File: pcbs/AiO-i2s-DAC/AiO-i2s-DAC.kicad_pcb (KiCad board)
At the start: 2 copper layers, 58.8 x 55.7 mm, 102 parts, among them J1 UART1, J2 SJ-3524-SMT-TR, J3 Audio Out, J4 UART0, J5 USB4105-GF-A, J6 USB4105-GF-A, J7 Conn_01x02, Q3 BC818, Q4 MBT3904DW1, Q6 MBT3904DW1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

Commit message: S3 insertion start
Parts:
- removed C10, C13, C15: 10uF 10V, Capacitor_SMD:C_0603_1608Metric
- removed C11, C14: 0.1uF 50V, Capacitor_SMD:C_0603_1608Metric
- removed D1, D11, D2, D9: 2.1V G 10mA, LED_SMD:LED_0603_1608Metric
- removed D14: 1N5819HW-7-F, DIY:SOD3716X145N
- removed D8: SP0503BAHTG, Package_TO_SOT_SMD:SOT-143
- removed DCD1, GND1: TestPoint_Small, TestPoint:TestPoint_Pad_D1.0mm
- removed J3: Audio Out, Connector_PinHeader_2.54mm:PinHeader_1x03_P2.54mm_Vertical
- removed J6: USB4105-GF-A, DIY:GCT_USB4105-GF-A
- removed JP1: ActDCD, Jumper:SolderJumper-3_P1.3mm_Bridged12_RoundedPad1.0x1.5mm
- removed R1, R2, R34, R35: 1K 1%, Resistor_SMD:R_0603_1608Metric
- removed R15, R23: 22.1K 1%, Resistor_SMD:R_0603_1608Metric
- removed R16, R24: 47.5K 1%, Resistor_SMD:R_0603_1608Metric
- removed R17, R25: 2K 1%, Resistor_SMD:R_0603_1608Metric
- removed R18, R19, R26, R27, R29: 0R, Resistor_SMD:R_0603_1608Metric
- removed R28, R30: 5.1K 1%, Resistor_SMD:R_0603_1608Metric
- removed U3, U4: CP2102-GM, Package_DFN_QFN:QFN-28-1EP_5x5mm_P0.5mm_EP3.35x3.35mm
- added D12: 2.1V G 10mA, LED_SMD:LED_0603_1608Metric, F.Cu at (213.5, 70.5)
- added D13: 2.1V G 10mA, LED_SMD:LED_0603_1608Metric, F.Cu at (213.5, 73.1)
- added D3: 2.1V G 10mA, LED_SMD:LED_0603_1608Metric, F.Cu at (213.5, 65.3)
- added D4: 2.1V G 10mA, LED_SMD:LED_0603_1608Metric, F.Cu at (213.5, 67.9)
- added DTR0: TestPoint_Small, TestPoint:TestPoint_Pad_D2.0mm, F.Cu at (209.4, 66.0)
- added HPD1: TestPoint_Small, TestPoint:TestPoint_Pad_D2.0mm, F.Cu at (209.4, 70.1)
- added JP4: HPD bypass, Jumper:SolderJumper-2_P1.3mm_Open_RoundedPad1.0x1.5mm, F.Cu at (217.6, 65.8)
- added R10: 1K 1%, Resistor_SMD:R_0603_1608Metric, F.Cu at (205.4, 70.3)
- added R11: 1K 1%, Resistor_SMD:R_0603_1608Metric, F.Cu at (205.4, 72.8)
- added R42: 10K 1%, Resistor_SMD:R_0603_1608Metric, F.Cu at (205.4, 75.3)
- added R43: 10K 1%, Resistor_SMD:R_0603_1608Metric, F.Cu at (205.4, 77.8)
- added R8: 1K 1%, Resistor_SMD:R_0603_1608Metric, F.Cu at (205.4, 65.3)
- added R9: 1K 1%, Resistor_SMD:R_0603_1608Metric, F.Cu at (205.4, 67.8)
- added RTS0: TestPoint_Small, TestPoint:TestPoint_Pad_D2.0mm, F.Cu at (209.4, 74.1)
- added U6: ESP32-S3, Package_DFN_QFN:QFN-56-1EP_7x7mm_P0.4mm_EP5.6x5.6mm, F.Cu at (216.1, 79.0)
- moved J4 39.1 mm to (213.0, 87.2)
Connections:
- net /CP2102_0/D+ renamed /usb_dp
- net /CP2102_0/D- renamed /usb_dn
- net Net-(C9-Pad2) renamed BOOT
- J1 pad 2: DCD -> AGND
- J2 pad TN: unconnected-(J2-PadTN) -> Net-(JP4-A)
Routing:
- net RXD1: track 67.9 -> 0.00 mm, vias 4 -> 0
- net +3.3V: track 183.6 -> 119.9 mm, vias 9 -> 2
- net TXD1: track 60.8 -> 3.66 mm, vias 6 -> 1
- net RXD0: track 42.9 -> 0.00 mm, vias 2 -> 0
- net DCD: track 42.7 -> 0.00 mm, vias 2 -> 0
- net TXD0: track 39.7 -> 0.00 mm, vias 2 -> 0
- net VBUS: track 55.4 -> 19.7 mm, vias 4 -> 2
- net DTR0: track 55.9 -> 22.2 mm, vias 3 -> 2
- net RTS0: track 47.8 -> 17.1 mm, vias 4 -> 3
- net Net-(J6-SHELL_GND): track 19.8 -> 0.00 mm
- net /CP2102-GM/D+: track 16.1 -> 0.00 mm, vias 3 -> 0
- net /CP2102-GM/D-: track 14.9 -> 0.00 mm, vias 2 -> 0
- net ROUT: track 18.9 -> 7.19 mm
- net LOUT: track 19.5 -> 13.9 mm
- net +5V: track 78.4 -> 73.2 mm, vias 3 -> 2
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
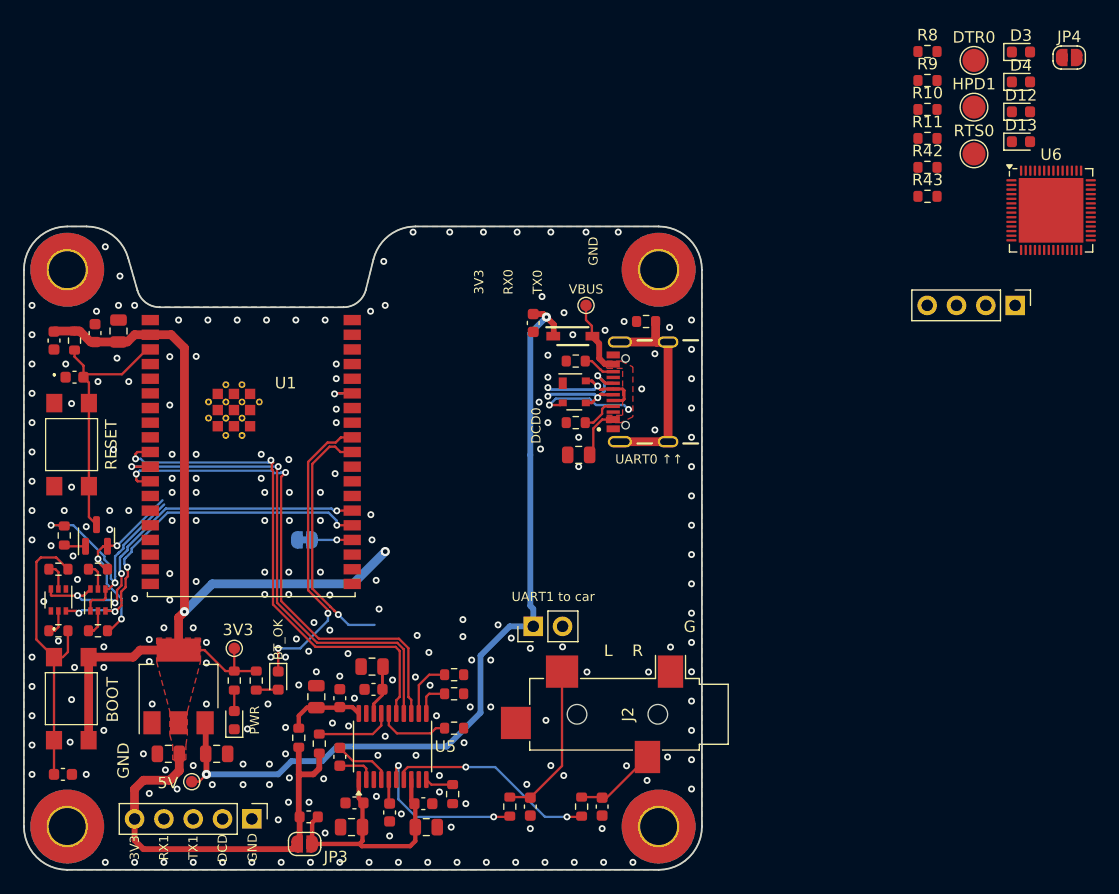
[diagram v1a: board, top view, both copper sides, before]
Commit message: Preliminary S3 version schematic and layout
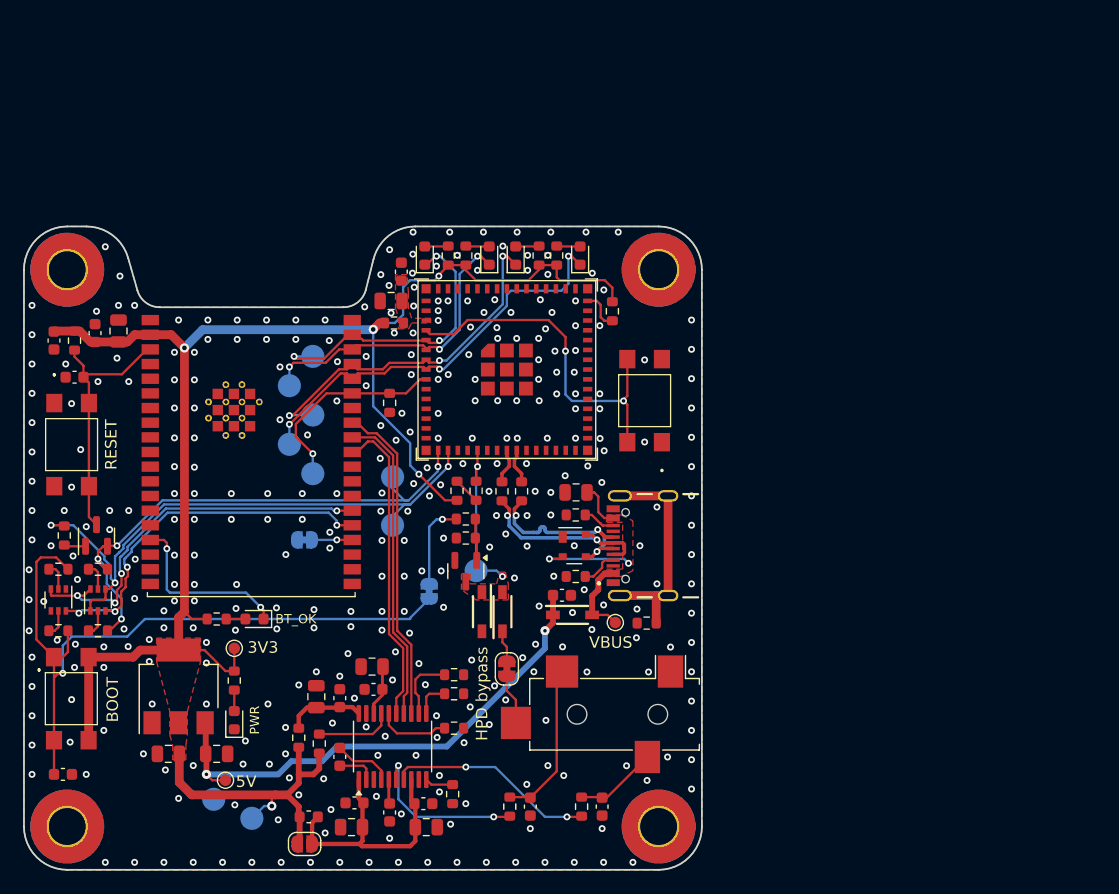
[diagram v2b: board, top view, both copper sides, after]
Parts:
- removed J1: UART1, Connector_PinHeader_2.54mm:PinHeader_1x05_P2.54mm_Vertical
- removed J4: UART0, Connector_PinHeader_2.54mm:PinHeader_1x04_P2.54mm_Vertical
- removed J7: Conn_01x02, Connector_PinHeader_2.54mm:PinHeader_1x02_P2.54mm_Vertical
- removed R42: 10K 1%, Resistor_SMD:R_0603_1608Metric
- removed U6: ESP32-S3, Package_DFN_QFN:QFN-56-1EP_7x7mm_P0.4mm_EP5.6x5.6mm
- added C30: 0.1uF 50V, Capacitor_SMD:C_0603_1608Metric, F.Cu at (159.8, 84.3)
- added C31: 10uF 16V, Capacitor_SMD:C_0805_2012Metric, F.Cu at (158.9, 86.9)
- added D11: 1N5819HW-7-F, DIY:SOD3716X145N, F.Cu at (166.8, 113.8)
- added D14: 1N5819HW-7-F, DIY:SOD3716X145N, F.Cu at (168.5, 113.8)
- added JP7: BOOT Bypass, Jumper:SolderJumper-2_P1.3mm_Bridged_RoundedPad1.0x1.5mm, B.Cu at (162.2, 112.0)
- added Q1: 2N7002, Package_TO_SOT_SMD:SOT-23, F.Cu at (165.4, 110.3)
- added R15: 1K 1%, Resistor_SMD:R_0603_1608Metric, F.Cu at (165.4, 105.8)
- added R44: 10K 1%, Resistor_SMD:R_0603_1608Metric, F.Cu at (158.8, 95.7)
- added R45: 0R, Resistor_SMD:R_0603_1608Metric, F.Cu at (159.1, 88.8)
- added R46: 0R, Resistor_SMD:R_0603_1608Metric, F.Cu at (178.1, 87.8)
- added R47: 0R, Resistor_SMD:R_0603_1608Metric, F.Cu at (168.5, 103.4)
- added R48: 0R, Resistor_SMD:R_0603_1608Metric, F.Cu at (170.2, 103.4)
- added R49: 10K 1%, Resistor_SMD:R_0603_1608Metric, F.Cu at (165.4, 107.4)
- added R50: 10K 1%, Resistor_SMD:R_0603_1608Metric, F.Cu at (164.6, 103.3)
- added S3: S3_BOOT, DIY:TL3305BF260QG, F.Cu at (180.8, 95.5)
- added TP1: 3V3, TestPoint:TestPoint_Pad_D2.0mm, B.Cu at (146.8, 131.7)
- added TP2: RXD1, TestPoint:TestPoint_Pad_D2.0mm, B.Cu at (150.1, 94.2)
- added TP3: TXD1, TestPoint:TestPoint_Pad_D2.0mm, B.Cu at (152.1, 91.7)
- added TP4: DCD, TestPoint:TestPoint_Pad_D2.0mm, B.Cu at (152.1, 101.8)
- added TP5: GND, TestPoint:TestPoint_Pad_D2.0mm, B.Cu at (143.5, 130.0)
- added TP6: RXD0, TestPoint:TestPoint_Pad_D2.0mm, B.Cu at (150.1, 99.3)
- added TP7: TXD0, TestPoint:TestPoint_Pad_D2.0mm, B.Cu at (152.1, 96.7)
- added U7: ESP32-S3-MINI-1U-Nx, PCM_Espressif:ESP32-S3-MINI-1U, F.Cu at (168.9, 92.8)
- JP4: footprint Jumper:SolderJumper-2_P1.3mm_Open_RoundedPad1.0x1.5mm -> Jumper:SolderJumper-2_P1.3mm_Bridged_RoundedPad1.0x1.5mm
- S1: value TL3305BF260QG -> ESP_BOOT
- S2: value TL3305BF260QG -> ESP_RESET
- TP10: renamed from RTS0; value TestPoint_Small -> RTS 0; moved to B.Cu
- TP11: renamed from 3V1; value TestPoint_Small -> 3V3
- TP12: renamed from 5V1; value TestPoint_Small -> 5V
- TP13: renamed from HPD1; value TestPoint_Small -> HP detect; moved to B.Cu
- TP8: renamed from VBUS1; value TestPoint_Small -> VBUS
- TP9: renamed from DTR0; value TestPoint_Small -> DTR 0; moved to B.Cu
- moved JP4 72.0 mm to (168.9, 118.7), turned to 90 degrees
- moved TP9 64.5 mm to (159.0, 106.3), turned to 180 degrees
- moved TP13 58.9 mm to (166.2, 110.2), turned to 180 degrees
- moved TP10 57.6 mm to (159.0, 102.1), turned to 180 degrees
- moved D13 52.6 mm to (161.8, 82.9), turned to 90 degrees
- moved D12 47.7 mm to (167.4, 82.9), turned to 90 degrees
- moved R43 46.7 mm to (166.2, 103.3), turned to -90 degrees
- moved D4 46.3 mm to (169.7, 82.9), turned to 90 degrees
- moved R11 42.8 mm to (163.8, 82.9), turned to 90 degrees
- moved D3 42.1 mm to (175.3, 82.9), turned to 90 degrees
- moved R10 42.0 mm to (165.4, 82.9), turned to 90 degrees
- moved R9 36.9 mm to (171.7, 82.9), turned to 90 degrees
- moved R8 36.7 mm to (173.2, 82.9), turned to 90 degrees
- moved TP8 27.6 mm to (178.3, 114.7)
- moved R21 26.1 mm to (181.0, 114.8)
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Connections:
- net /usb_dn renamed /USB_DN
- net /usb_dp renamed /USB_DP
- net HP_DETECT renamed ~{HP_DETECT}
- D6 pad 1: IO18 -> ~{BT_ST}
- R43 pad 2: +3.3V -> Net-(R43-Pad2)
- U1 pad 10: WSEL -> unconnected-(U1-DAC_1/ADC2_CH8/GPIO25-Pad10)
- U1 pad 11: DIN -> unconnected-(U1-DAC_2/ADC2_CH9/GPIO26-Pad11)
- U1 pad 12: BCLK -> unconnected-(U1-ADC2_CH7/GPIO27-Pad12)
- U1 pad 16: unconnected-(U1-MTCK/GPIO13/ADC2_CH4-Pad16) -> ~{BT_ST}
- U1 pad 29: IO5 -> WSEL
- U1 pad 30: IO18 -> DIN
- U1 pad 31: RXD1 -> BCLK
- U1 pad 33: TXD1 -> DCD
- U1 pad 36: unconnected-(U1-GPIO22-Pad36) -> RXD1
- U1 pad 37: unconnected-(U1-GPIO23-Pad37) -> TXD1
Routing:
- net +3.3V: track 119.9 -> 157.5 mm, vias 2 -> 5
- net BOOT: track 25.6 -> 62.4 mm, vias 0 -> 1
- net RXD0: track 0.00 -> 36.0 mm, vias 0 -> 3
- net Net-(U7-IO0): track 0.00 -> 31.0 mm, vias 0 -> 2
- net TXD0: track 0.00 -> 30.7 mm, vias 0 -> 3
- net DTR0: track 22.2 -> 52.4 mm, vias 2 -> 3
- net RTS0: track 17.1 -> 46.7 mm, vias 3 -> 4
- net +5V: track 73.2 -> 45.1 mm
- net RXD1: track 0.00 -> 26.6 mm, vias 0 -> 3
- net IO18: track 26.5 -> 0.00 mm, vias 2 -> 0
- net TXD1: track 3.66 -> 25.8 mm, vias 1 -> 3
- net IO5: track 21.8 -> 0.00 mm, vias 1 -> 0
- net DCD: track 0.00 -> 17.8 mm, vias 0 -> 1
- net WSEL: track 44.6 -> 27.1 mm, vias 2 -> 0
- net DIN: track 44.4 -> 27.2 mm, vias 2 -> 0
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- added copper zone on F.Cu, net Net-(U7-3V3)
- added copper zone on F.Cu, net ~{HP_DETECT}
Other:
- board text removed: "DCD"
- board text removed: "DCD0"
- board text removed: "G"
- board text removed: "GND"
- board text removed: "IO5"
- board text removed: "L"
- board text removed: "R"
- board text removed: "RX0"
- board text removed: "RX1"
- board text removed: "TX0"
- board text removed: "TX1"
- board text removed: "UART0 ↑↑"
- board text removed: "UART1 to car"
- board text removed: "VBUS"
